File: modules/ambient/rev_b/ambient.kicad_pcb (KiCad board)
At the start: 2 copper layers, 68.1 x 66 mm, 60 parts, among them P1 CONN_01X03, P2 CONN_01X06, P3 SIGNPOST_MODULE_GENERIC, P4 JLINK-TC, P5 CONN_01X06, SW1 BSU-1000P, U1 LPS25HB, U2 TPS62086, U3 LPS35HW, U4 SAM4LC8A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

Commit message: updated silkcreen
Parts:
- moved G*** 15.2 mm to (103.0, 107.1)
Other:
- board text added: "Ambient Sensor Module Rev B Sensor Types: Temperature Pressure Humidity Light"
- board text added: "wwhuang 2016"
- board text removed: "Ambient_revB Huang, 2016"
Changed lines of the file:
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@@
     (area 88.9 59.84875 165.100001 142.1626)
     (thickness 1.6)
-    (drawings 37)
+    (drawings 38)
     (tracks 705)
     (zones 0)
@@
     (tags "smd diode")
     (attr smd)
-    (fp_text reference D1 (at 0 1.5 270) (layer F.SilkS)
+    (fp_text reference D1 (at 0.1524 -1.2446 270) (layer F.SilkS)
       (effects (font (size 0.762 0.762) (thickness 0.15)))
     )
@@
     (tags "smd diode")
     (attr smd)
-    (fp_text reference D2 (at 0.0136 1.27 270) (layer F.SilkS)
+    (fp_text reference D2 (at 0.127 -1.3208 270) (layer F.SilkS)
       (effects (font (size 0.762 0.762) (thickness 0.15)))
     )
@@
     (tags "smd diode")
     (attr smd)
-    (fp_text reference D3 (at 0 1.2446 270) (layer F.SilkS)
+    (fp_text reference D3 (at 0.2286 -1.4478 270) (layer F.SilkS)
       (effects (font (size 0.762 0.762) (thickness 0.15)))
     )
@@
     (tags "resistor 0402")
     (attr smd)
-    (fp_text reference R9 (at 0.0254 -1.1684 90) (layer F.SilkS)
+    (fp_text reference R9 (at 1.8034 0.0508 90) (layer F.SilkS)
       (effects (font (size 0.762 0.762) (thickness 0.15)))
     )
@@
     (tags "resistor 0402")
     (attr smd)
-    (fp_text reference R10 (at 0 -1.1938 90) (layer F.SilkS)
+    (fp_text reference R10 (at 2.1264 0.0508 90) (layer F.SilkS)
       (effects (font (size 0.762 0.762) (thickness 0.15)))
     )
@@
   )
   (module lab11-logos:BlockM (layer F.Cu)
-    (at 112.1918 119.253)
+    (at 103.0224 107.0864)
     (fp_text reference G*** (at 0 0) (layer F.SilkS) hide
       (effects (font (thickness 0.3)))
@@
       (net 3 +3V3))
   )
+  (gr_text "Ambient Sensor Module\nRev B\nSensor Types: \nTemperature \nPressure\nHumidity\nLight \n\n\n" (at 111.9886 123.4948) (layer F.SilkS)
+    (effects (font (size 1.27 1.27) (thickness 0.1905)))
+  )
   (gr_circle (center 148.2344 114.767219) (end 148.3106 114.818019) (layer F.SilkS) (width 0.2))
   (gr_circle (center 134.274419 115.1128) (end 134.350619 115.1636) (layer F.SilkS) (width 0.2))
@@
     (effects (font (size 0.762 0.762) (thickness 0.1905)))
   )
-  (gr_text "Ambient_revB\nHuang, 2016" (at 109.5502 110.6932) (layer F.SilkS)
-    (effects (font (size 1.27 1.27) (thickness 0.3)))
+  (gr_text "wwhuang\n2016" (at 157.861 114.1476) (layer F.SilkS)
+    (effects (font (size 0.762 0.762) (thickness 0.1905)))
   )
   (gr_text GND (at 150.9776 90.1446 270) (layer F.SilkS)

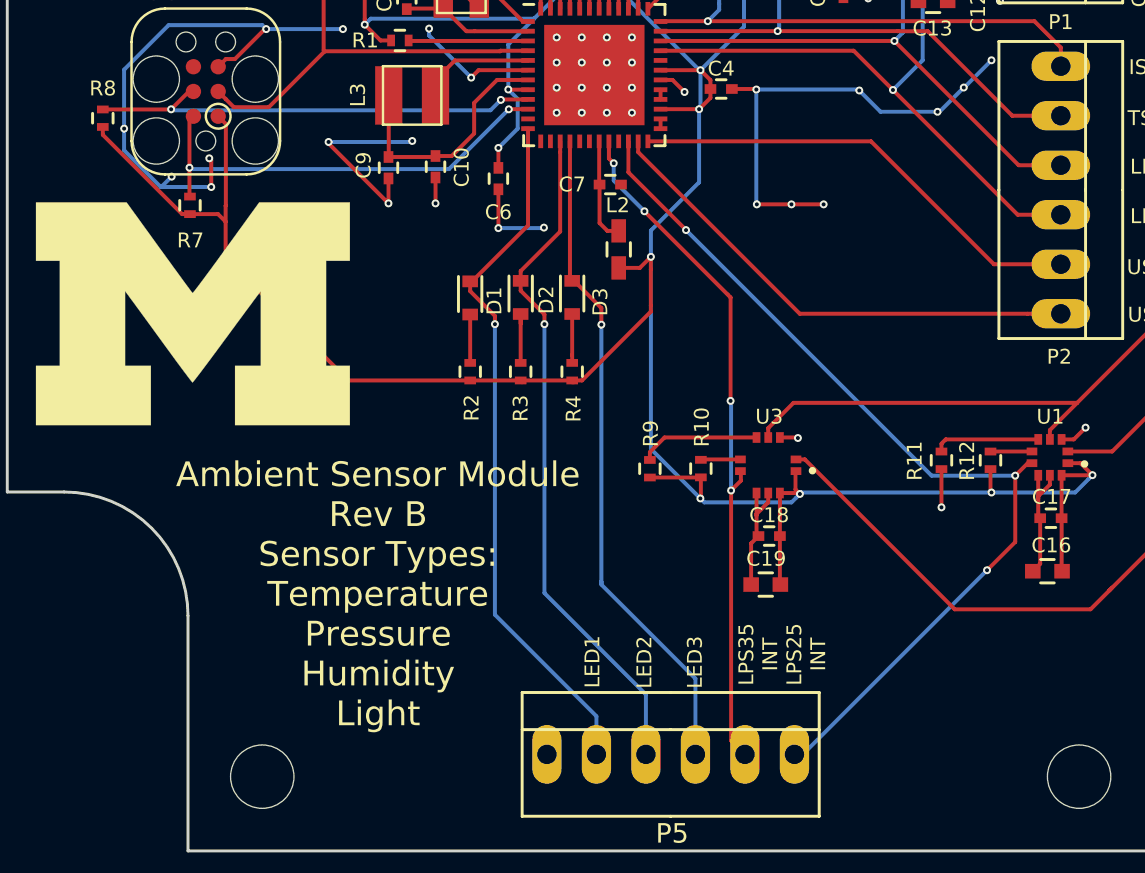
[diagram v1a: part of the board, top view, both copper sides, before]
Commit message: added pir sensor
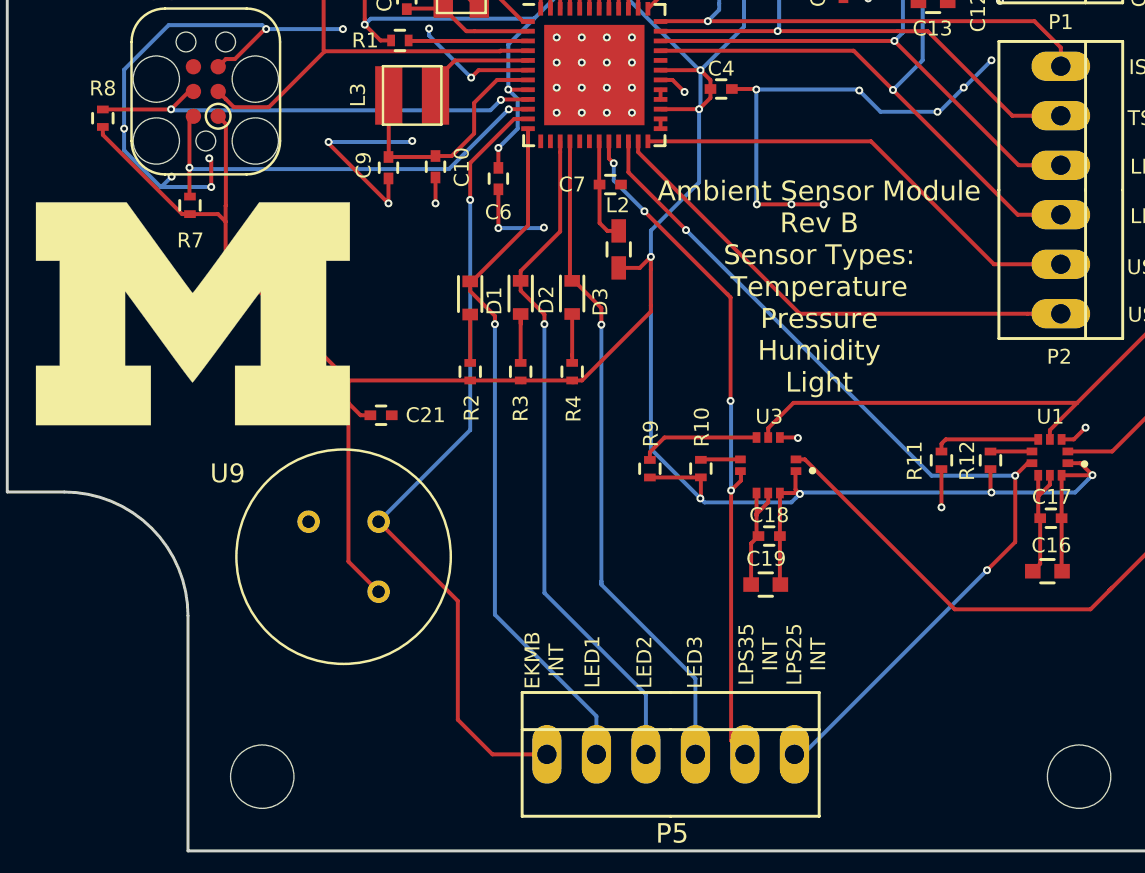
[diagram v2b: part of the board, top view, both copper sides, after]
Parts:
- added C21: C_0.1u_0402_10V_10%_JB, Capacitors_SMD:C_0402, F.Cu at (112.1, 112.3)
- added U9: EKMB1101111, lab11-ic:EKMB1101111, F.Cu at (110.2, 119.5)
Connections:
- P5 pad 1: Net-(P5-Pad1) -> /EKMB_INT
- U4 pad 11: Net-(U4-Pad11) -> /EKMB_INT
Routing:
- net /EKMB_INT: track 0.00 -> 41.4 mm, vias 0 -> 1
- net +3V3: track 254.4 -> 267.3 mm
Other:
- board text added: "EKMB INT"

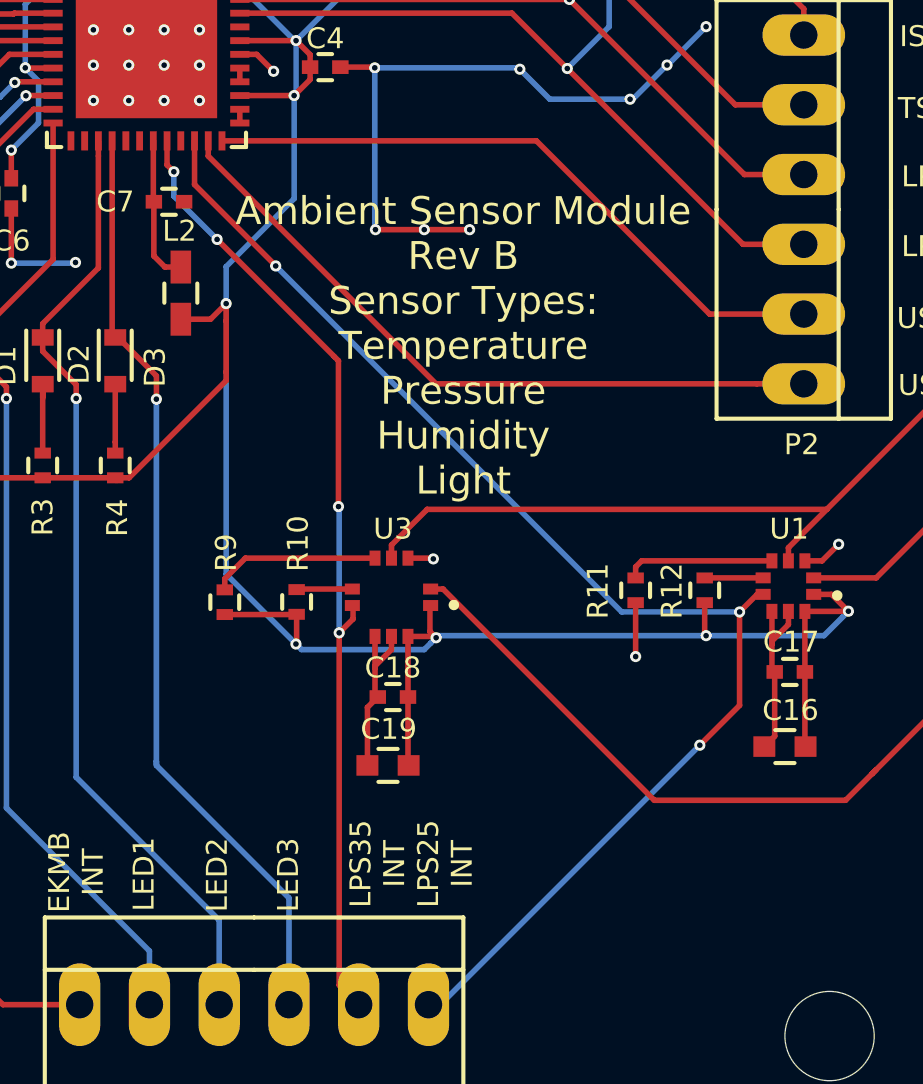
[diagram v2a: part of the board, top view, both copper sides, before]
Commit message: slight fix to grounnd plane
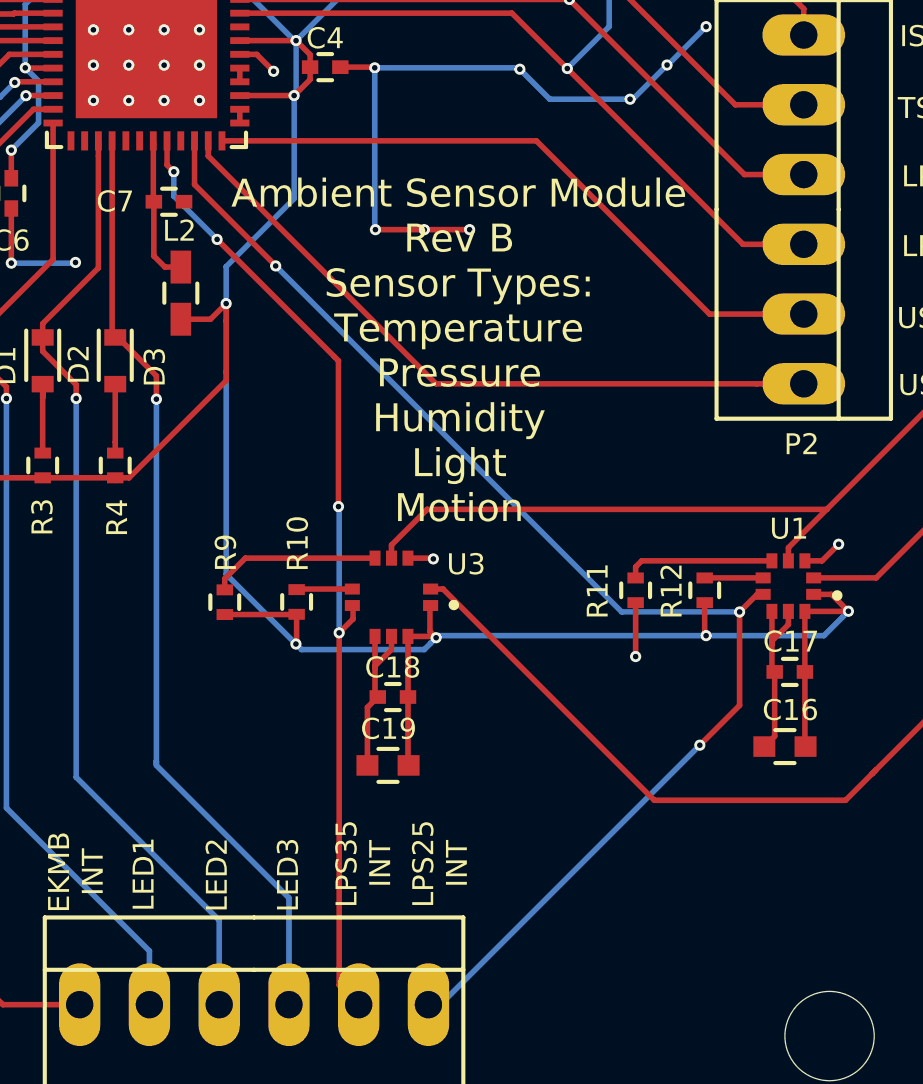
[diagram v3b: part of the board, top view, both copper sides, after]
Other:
- board text added: "Ambient Sensor Module Rev B Sensor Types: Temperature Pressure Humidity Light Motion"
- board text removed: "Ambient Sensor Module Rev B Sensor Types: Temperature Pressure Humidity Light"
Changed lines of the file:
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@@
     (last_trace_width 0.2032)
     (trace_clearance 0.1524)
-    (zone_clearance 0.2032)
+    (zone_clearance 0.127)
     (zone_45_only no)
     (trace_min 0.1016)
@@
   (module lab11-ic:CCLGA-10L_3.5x3.5mm (layer F.Cu)
     (at 132.0038 114.8334)
-    (fp_text reference U3 (at 0.0508 -2.4892) (layer F.SilkS)
+    (fp_text reference U3 (at 2.7178 -1.1938) (layer F.SilkS)
       (effects (font (size 0.762 0.762) (thickness 0.127)))
     )
@@
     (effects (font (size 0.762 0.762) (thickness 0.1905)))
   )
-  (gr_text "Ambient Sensor Module\nRev B\nSensor Types: \nTemperature \nPressure\nHumidity\nLight \n\n\n" (at 134.62 107.315) (layer F.SilkS)
+  (gr_text "Ambient Sensor Module\nRev B\nSensor Types: \nTemperature \nPressure\nHumidity\nLight \nMotion\n\n" (at 134.4676 106.68) (layer F.SilkS)
     (effects (font (size 1.016 1.016) (thickness 0.1905)))
   )
@@
     (effects (font (size 0.762 0.762) (thickness 0.1905)))
   )
-  (gr_text "LPS35\nINT" (at 131.4958 124.5362 90) (layer F.SilkS)
+  (gr_text "LPS35\nINT" (at 130.9878 124.5362 90) (layer F.SilkS)
     (effects (font (size 0.762 0.762) (thickness 0.1905)))
   )
-  (gr_text "LPS25\nINT" (at 133.9596 124.5362 90) (layer F.SilkS)
+  (gr_text "LPS25\nINT" (at 133.7818 124.5362 90) (layer F.SilkS)
     (effects (font (size 0.762 0.762) (thickness 0.1905)))
   )
@@
   (segment (start 116.078 121.793) (end 116.078 127.889) (width 0.2032) (layer F.Cu) (net 60))
   (zone (net 2) (net_name GND) (layer B.Cu) (hatch edge 0.508)
-    (connect_pads (clearance 0.2032))
-    (min_thickness 0.254)
+    (connect_pads (clearance 0.127))
+    (min_thickness 0.127)
     (fill yes (arc_segments 16) (thermal_gap 0.508) (thermal_bridge_width 0.508))
     (polygon
